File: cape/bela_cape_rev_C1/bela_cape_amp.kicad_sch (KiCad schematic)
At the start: 16 parts, among them IC4 LM4876, IC5 LM4876

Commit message: Further routing on C1 cape
(cherry picked from commit 232a25b01e013bf194cdc3a343766aa7b43870aa)
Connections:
- net +5V renamed +5VP
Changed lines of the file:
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@@
     (pin "1")
   )
-  (symbol (lib_id "power:+5V") (at 83.82 27.94 0) (unit 1)
+  (symbol (lib_id "power:+5VP") (at 83.82 27.94 0) (unit 1)
     (in_bom yes) (on_board yes) (fields_autoplaced)
-    (property "Reference" "#PWR028" (id 0) (at 83.82 31.75 0)
+    (property "Reference" "#PWR0157" (id 0) (at 83.82 31.75 0)
       (effects (font (size 1.27 1.27)) hide)
     )
-    (property "Value" "+5V" (id 1) (at 83.82 24.3642 0))
+    (property "Value" "+5VP" (id 1) (at 83.82 24.3642 0))
     (property "Footprint" "" (id 2) (at 83.82 27.94 0)
       (effects (font (size 1.27 1.27)) hide)

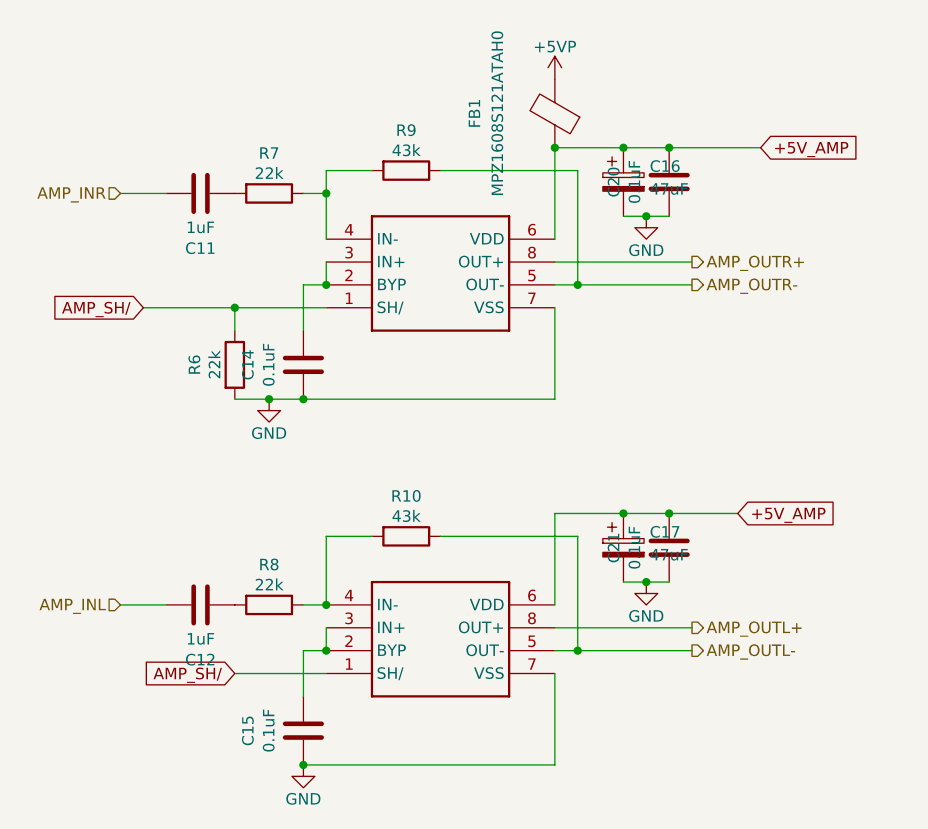
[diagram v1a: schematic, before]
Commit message: First complete routing of C1 cape
(cherry picked from commit 8c5092941a0b3ec42f55098733fd0108b2086674)
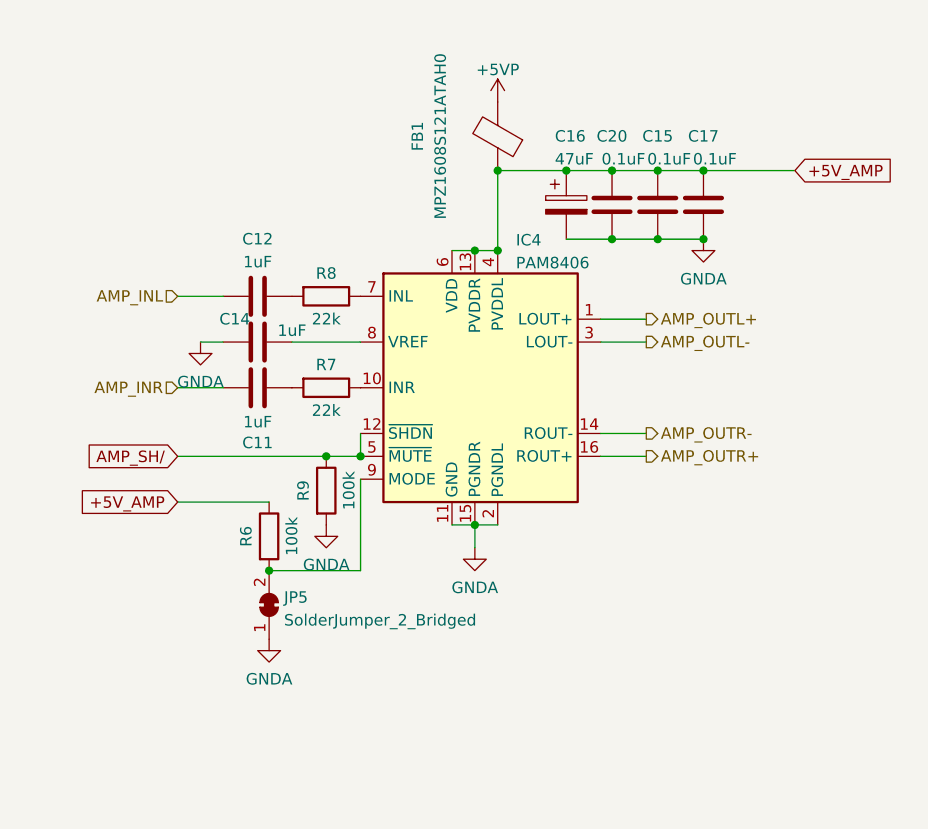
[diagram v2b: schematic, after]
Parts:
- removed C17: 47uF, Capacitor_SMD:C_1206_3216Metric, symbol Device:C_Polarized
- removed C21: 0.1uF, Capacitor_SMD:C_0603_1608Metric, symbol Device:C
- removed IC4, IC5: LM4876, bela_cape:SO8, symbol bela_cape-eagle-import:LM4876
- removed R10: 43k, Resistor_SMD:R_0603_1608Metric, symbol Device:R
- added C17: 0.1uF, Capacitor_SMD:C_0603_1608Metric, symbol Device:C
- added IC4: PAM8406, Package_SO:SO-16_3.9x9.9mm_P1.27mm, symbol Bela:PAM8406
- added JP5: SolderJumper_2_Bridged, Jumper:SolderJumper-2_P1.3mm_Bridged_Pad1.0x1.5mm, symbol Jumper:SolderJumper_2_Bridged
- C14: value 0.1uF -> 1uF
- R6: value 22k -> 100k
- R9: value 43k -> 100k
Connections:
- net +5V_AMP: now also C15.2, R6.1, C17.2, IC4.13 (PVDDR), IC4.4 (PVDDL), IC4.6 (VDD)
- net AMP_OUTL+: now also IC4.1 (LOUT+)
- net AMP_OUTL-: now also IC4.3 (LOUT-)
- net AMP_OUTR+: now also IC4.16 (ROUT+)
- net AMP_OUTR-: now also IC4.14 (ROUT-); no longer R9.1
- net AMP_SH/: now also R9.1, IC4.12 (~{SHDN}), IC4.5 (~{MUTE}); no longer R6.1
- net at R8.1: now also IC4.7 (INL)
- net at R7.1: now also IC4.10 (INR); no longer R9.2
- net GNDA: now reaches C14.2
- net GNDA: now also C15.1, C16.2, C20.1, R9.2, C17.1, IC4.11 (GND), IC4.15 (PGNDR), IC4.2 (PGNDL), JP5.1 (A)
- removed net GND: C14.1, C15.1, C16.2, C20.1, R6.2
- new net: IC4.9 (MODE), JP5.2 (B), R6.2
- new net: C14.1, IC4.8 (VREF)
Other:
- moved on the sheet: C11, C12, C16, C20, FB1, R7, R8

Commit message: Bela cape C1: renumber components
(cherry picked from commit 6ebfe9c44bb7559ffb4c9dbd092e49803523e6a1)
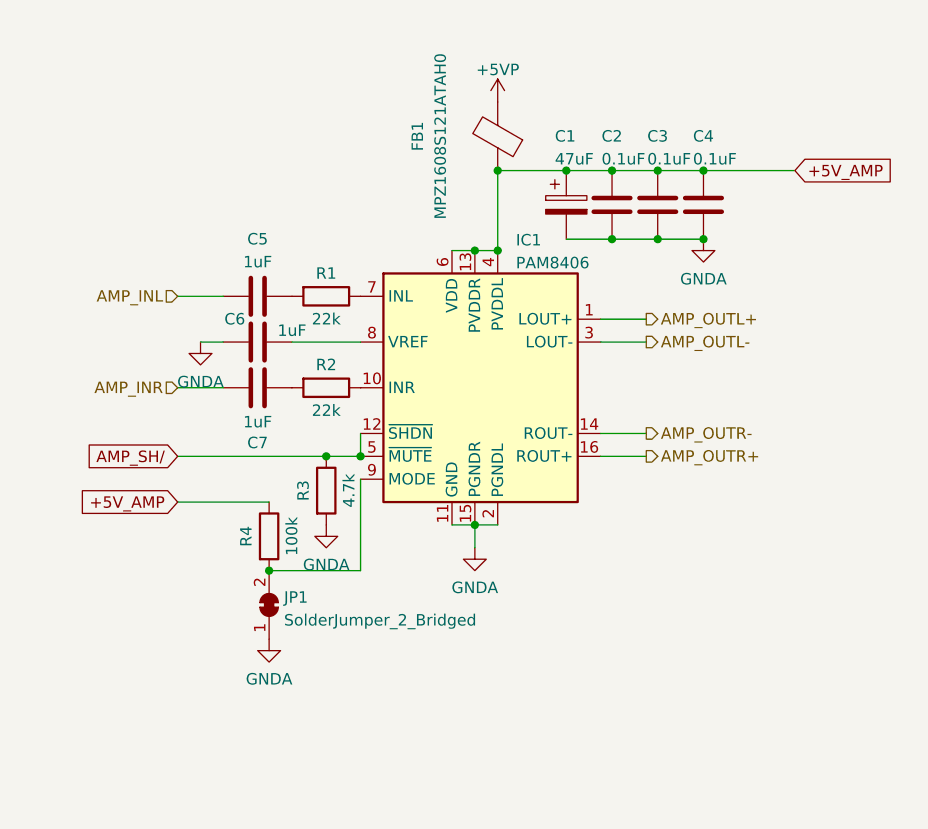
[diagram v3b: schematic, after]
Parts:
- R3: renamed from R9; value 100k -> 4.7k
- renumbered C16 to C1, C20 to C2, C15 to C3, C17 to C4, C12 to C5, C14 to C6, C11 to C7, IC4 to IC1, JP5 to JP1, R8 to R1, R7 to R2, R6 to R4
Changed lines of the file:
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@@
   (symbol (lib_id "power:GNDA") (at 100.33 45.72 0) (unit 1)
     (in_bom yes) (on_board yes) (fields_autoplaced)
-    (property "Reference" "#PWR0173" (id 0) (at 100.33 52.07 0)
+    (property "Reference" "#PWR02" (id 0) (at 100.33 52.07 0)
       (effects (font (size 1.27 1.27)) hide)
     )
@@
   (symbol (lib_id "power:GNDA") (at 52.07 90.17 0) (unit 1)
     (in_bom yes) (on_board yes) (fields_autoplaced)
-    (property "Reference" "#PWR0172" (id 0) (at 52.07 96.52 0)
+    (property "Reference" "#PWR06" (id 0) (at 52.07 96.52 0)
       (effects (font (size 1.27 1.27)) hide)
     )
@@
   (symbol (lib_id "Device:R") (at 52.07 78.74 0) (unit 1)
     (in_bom yes) (on_board yes)
-    (property "Reference" "R6" (id 0) (at 49.53 78.74 90))
+    (property "Reference" "R4" (id 0) (at 49.53 78.74 90))
     (property "Value" "100k" (id 1) (at 54.61 78.74 90))
     (property "Footprint" "Resistor_SMD:R_0603_1608Metric" (id 2) (at 50.292 78.74 90)
@@
   (symbol (lib_id "Device:C") (at 95.25 41.91 180) (unit 1)
     (in_bom yes) (on_board yes)
-    (property "Reference" "C15" (id 0) (at 95.25 34.29 0))
+    (property "Reference" "C3" (id 0) (at 95.25 34.29 0))
     (property "Value" "0.1uF" (id 1) (at 96.52 36.83 0))
     (property "Footprint" "Capacitor_SMD:C_0603_1608Metric" (id 2) (at 94.2848 38.1 0)
@@
   (symbol (lib_id "power:+5VP") (at 77.47 30.48 0) (unit 1)
     (in_bom yes) (on_board yes) (fields_autoplaced)
-    (property "Reference" "#PWR0157" (id 0) (at 77.47 34.29 0)
+    (property "Reference" "#PWR01" (id 0) (at 77.47 34.29 0)
       (effects (font (size 1.27 1.27)) hide)
     )
@@
   (symbol (lib_id "Device:R") (at 58.42 62.23 270) (unit 1)
     (in_bom yes) (on_board yes)
-    (property "Reference" "R7" (id 0) (at 58.42 59.69 90))
+    (property "Reference" "R2" (id 0) (at 58.42 59.69 90))
     (property "Value" "22k" (id 1) (at 58.42 64.77 90))
     (property "Footprint" "Resistor_SMD:R_0603_1608Metric" (id 2) (at 58.42 60.452 90)
@@
   (symbol (lib_id "Device:R") (at 58.42 73.66 0) (unit 1)
     (in_bom yes) (on_board yes)
-    (property "Reference" "R9" (id 0) (at 55.88 73.66 90))
-    (property "Value" "100k" (id 1) (at 60.96 73.66 90))
+    (property "Reference" "R3" (id 0) (at 55.88 73.66 90))
+    (property "Value" "4.7k" (id 1) (at 60.96 73.66 90))
     (property "Footprint" "Resistor_SMD:R_0603_1608Metric" (id 2) (at 56.642 73.66 90)
       (effects (font (size 1.27 1.27)) hide)
@@
   (symbol (lib_id "Device:C") (at 100.33 41.91 180) (unit 1)
     (in_bom yes) (on_board yes)
-    (property "Reference" "C17" (id 0) (at 100.33 34.29 0))
+    (property "Reference" "C4" (id 0) (at 100.33 34.29 0))
     (property "Value" "0.1uF" (id 1) (at 101.6 36.83 0))
     (property "Footprint" "Capacitor_SMD:C_0603_1608Metric" (id 2) (at 99.3648 38.1 0)
@@
   (symbol (lib_id "power:GNDA") (at 44.45 57.15 0) (unit 1)
     (in_bom yes) (on_board yes) (fields_autoplaced)
-    (property "Reference" "#PWR0171" (id 0) (at 44.45 63.5 0)
+    (property "Reference" "#PWR03" (id 0) (at 44.45 63.5 0)
       (effects (font (size 1.27 1.27)) hide)
     )
@@
   (symbol (lib_id "power:GNDA") (at 58.42 77.47 0) (unit 1)
     (in_bom yes) (on_board yes) (fields_autoplaced)
-    (property "Reference" "#PWR0174" (id 0) (at 58.42 83.82 0)
+    (property "Reference" "#PWR04" (id 0) (at 58.42 83.82 0)
       (effects (font (size 1.27 1.27)) hide)
     )
@@
   (symbol (lib_id "Device:R") (at 58.42 52.07 270) (unit 1)
     (in_bom yes) (on_board yes)
-    (property "Reference" "R8" (id 0) (at 58.42 49.53 90))
+    (property "Reference" "R1" (id 0) (at 58.42 49.53 90))
     (property "Value" "22k" (id 1) (at 58.42 54.61 90))
     (property "Footprint" "Resistor_SMD:R_0603_1608Metric" (id 2) (at 58.42 50.292 90)
@@
   (symbol (lib_id "power:GNDA") (at 74.93 80.01 0) (unit 1)
     (in_bom yes) (on_board yes) (fields_autoplaced)
-    (property "Reference" "#PWR0170" (id 0) (at 74.93 86.36 0)
+    (property "Reference" "#PWR05" (id 0) (at 74.93 86.36 0)
       (effects (font (size 1.27 1.27)) hide)
     )
@@
   (symbol (lib_id "Device:C") (at 50.8 57.15 270) (unit 1)
     (in_bom yes) (on_board yes)
-    (property "Reference" "C14" (id 0) (at 48.26 54.61 90))
+    (property "Reference" "C6" (id 0) (at 48.26 54.61 90))
     (property "Value" "1uF" (id 1) (at 54.61 55.88 90))
     (property "Footprint" "Capacitor_SMD:C_0603_1608Metric" (id 2) (at 46.99 58.1152 0)
@@
   (symbol (lib_id "Device:C") (at 90.17 41.91 180) (unit 1)
     (in_bom yes) (on_board yes)
-    (property "Reference" "C20" (id 0) (at 90.17 34.29 0))
+    (property "Reference" "C2" (id 0) (at 90.17 34.29 0))
     (property "Value" "0.1uF" (id 1) (at 91.44 36.83 0))
     (property "Footprint" "Capacitor_SMD:C_0603_1608Metric" (id 2) (at 89.2048 38.1 0)
@@
   (symbol (lib_id "Device:C") (at 50.8 62.23 270) (unit 1)
     (in_bom yes) (on_board yes)
-    (property "Reference" "C11" (id 0) (at 50.8 68.3555 90))
+    (property "Reference" "C7" (id 0) (at 50.8 68.3555 90))
     (property "Value" "1uF" (id 1) (at 50.8 66.04 90))
     (property "Footprint" "Capacitor_SMD:C_0603_1608Metric" (id 2) (at 46.99 63.1952 0)
@@
   (symbol (lib_id "Bela:PAM8406") (at 74.93 60.96 0) (unit 1)
     (in_bom yes) (on_board yes) (fields_autoplaced)
-    (property "Reference" "IC4" (id 0) (at 79.4894 45.8302 0)
+    (property "Reference" "IC1" (id 0) (at 79.4894 45.8302 0)
       (effects (font (size 1.27 1.27)) (justify left))
     )
@@
   (symbol (lib_id "Device:C_Polarized") (at 85.09 41.91 0) (unit 1)
     (in_bom yes) (on_board yes)
-    (property "Reference" "C16" (id 0) (at 83.82 34.29 0)
+    (property "Reference" "C1" (id 0) (at 83.82 34.29 0)
       (effects (font (size 1.27 1.27)) (justify left))
     )
@@
   (symbol (lib_id "Jumper:SolderJumper_2_Bridged") (at 52.07 86.36 90) (unit 1)
     (in_bom yes) (on_board yes) (fields_autoplaced)
-    (property "Reference" "JP5" (id 0) (at 53.721 85.5253 90)
+    (property "Reference" "JP1" (id 0) (at 53.721 85.5253 90)
       (effects (font (size 1.27 1.27)) (justify right))
     )
@@
   (symbol (lib_id "Device:C") (at 50.8 52.07 270) (unit 1)
     (in_bom yes) (on_board yes)
-    (property "Reference" "C12" (id 0) (at 50.8 45.72 90))
+    (property "Reference" "C5" (id 0) (at 50.8 45.72 90))
     (property "Value" "1uF" (id 1) (at 50.8 48.26 90))
     (property "Footprint" "Capacitor_SMD:C_0603_1608Metric" (id 2) (at 46.99 53.0352 0)

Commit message: First complete iteration of C1 cape layout
(cherry picked from commit 0ee733c70b42f416809330055e007cefcdb105fa)
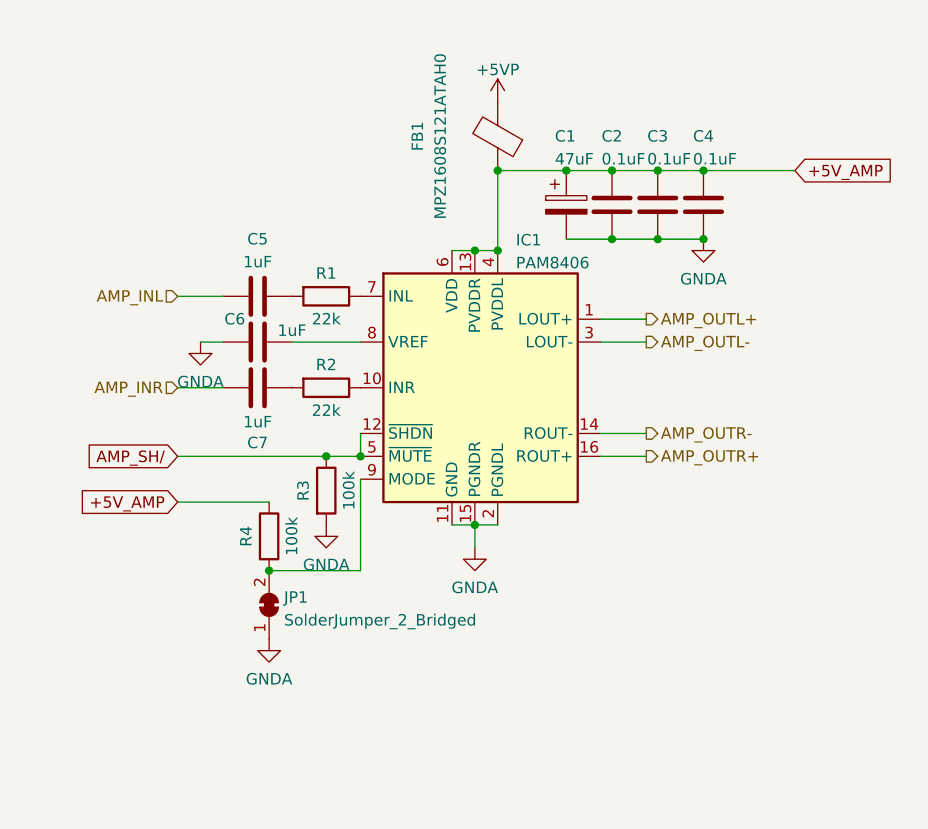
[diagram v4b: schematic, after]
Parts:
- R3: value 4.7k -> 100k
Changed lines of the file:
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@@
     (in_bom yes) (on_board yes)
     (property "Reference" "R3" (id 0) (at 55.88 73.66 90))
-    (property "Value" "4.7k" (id 1) (at 60.96 73.66 90))
+    (property "Value" "100k" (id 1) (at 60.96 73.66 90))
     (property "Footprint" "Resistor_SMD:R_0603_1608Metric" (id 2) (at 56.642 73.66 90)
       (effects (font (size 1.27 1.27)) hide)
